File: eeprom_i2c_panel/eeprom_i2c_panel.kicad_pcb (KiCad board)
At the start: 2 copper layers, 69 x 91 mm, 28 parts, among them J1 Conn_01x03_Pin, J2 Conn_01x03_Pin, J3 Conn_01x03_Pin, J4 1x4 strip 2.54mm, U1 24LC256

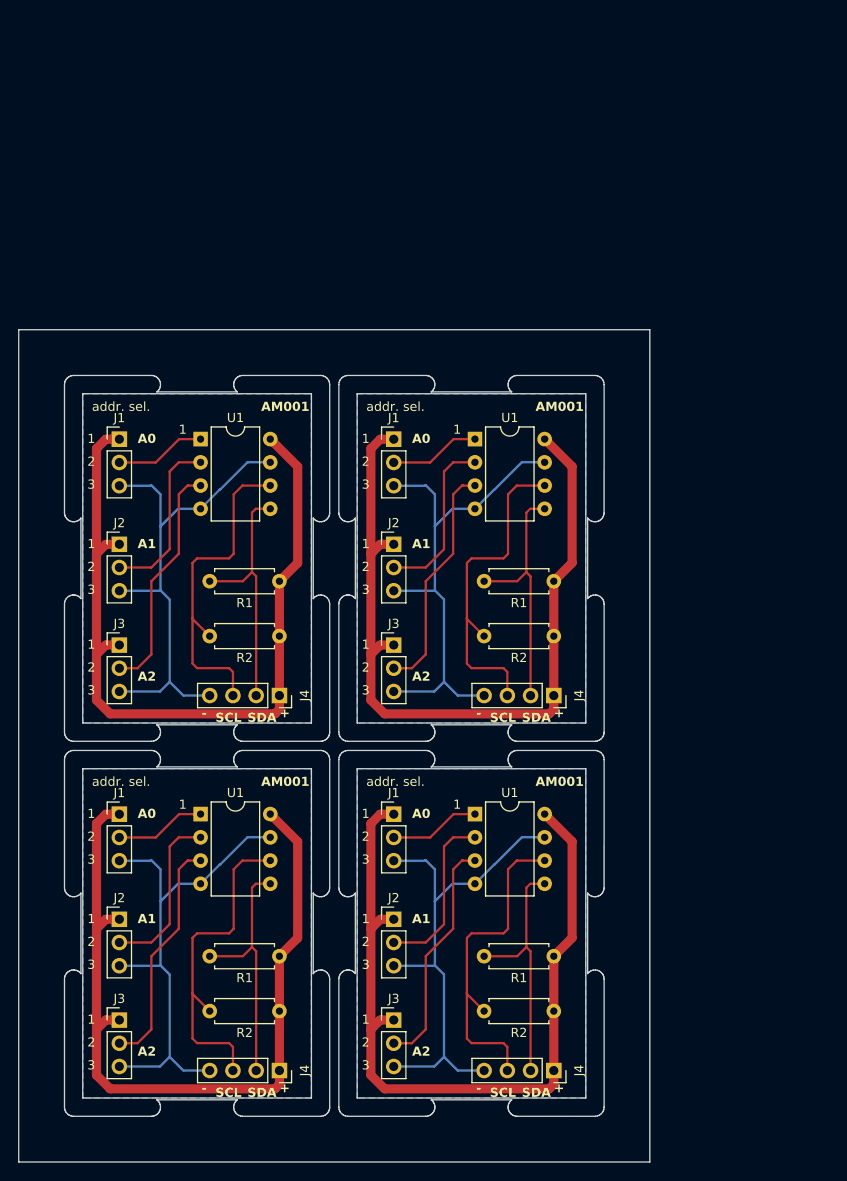
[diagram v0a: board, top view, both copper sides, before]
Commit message: Add by-pass capacitor; add mounting hole and change main connector's pinout.
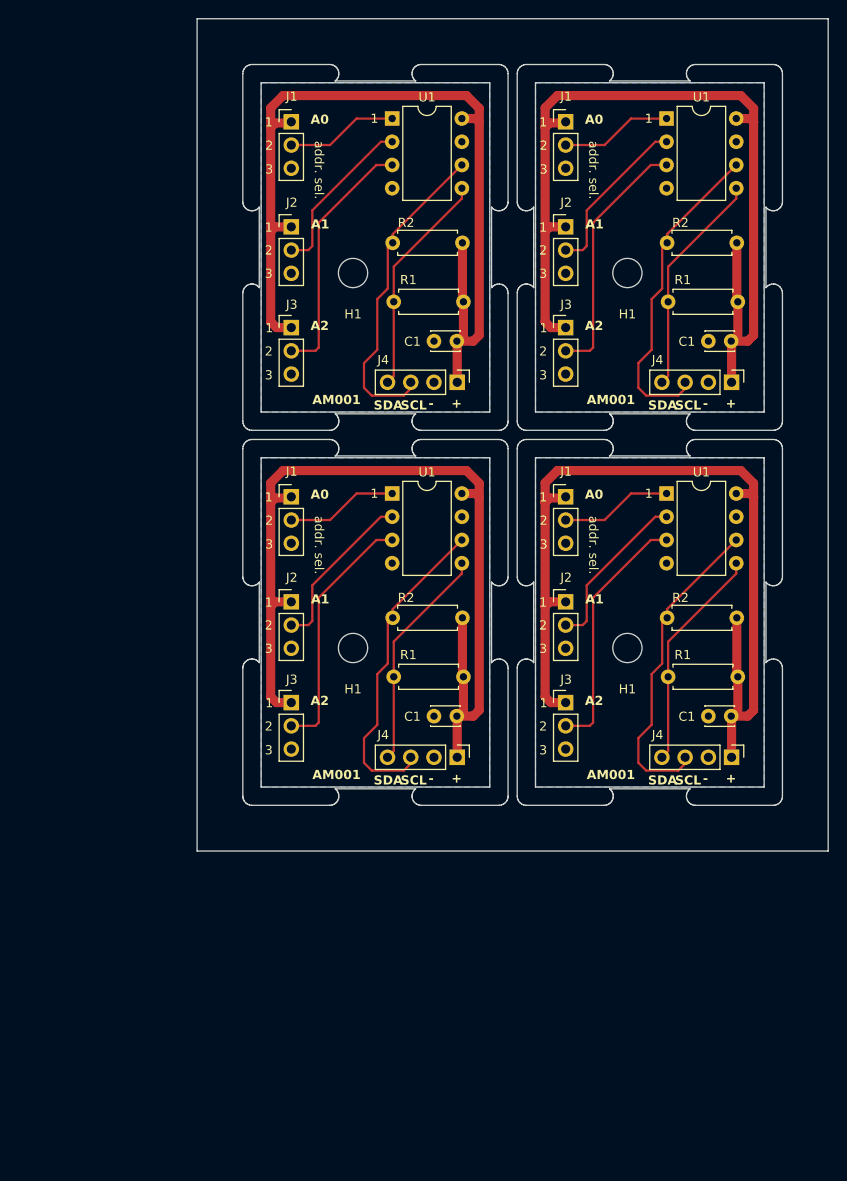
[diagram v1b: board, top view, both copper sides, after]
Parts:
- removed the J1 at (135.5, 66.0)
- removed the J1 at (105.5, 66.0)
- removed the J1 at (105.5, 107.0)
- removed the J1 at (135.5, 107.0)
- removed the J2 at (105.5, 77.5)
- removed the J2 at (135.5, 77.5)
- removed the J2 at (105.5, 118.5)
- removed the J2 at (135.5, 118.5)
- removed the J3 at (135.5, 129.5)
- removed the J3 at (105.5, 88.5)
- removed the J3 at (105.5, 129.5)
- removed the J3 at (135.5, 88.5)
- removed the J4 at (153.0, 94.0)
- removed the J4 at (123.0, 94.0)
- removed the J4 at (123.0, 135.0)
- removed the J4 at (153.0, 135.0)
- removed the R1 at (153.0, 81.5)
- removed the R1 at (153.0, 122.5)
- removed the R1 at (123.0, 81.5)
- removed the R1 at (123.0, 122.5)
- removed the R2 at (123.0, 87.5)
- removed the R2 at (153.0, 87.5)
- removed the R2 at (123.0, 128.5)
- removed the R2 at (153.0, 128.5)
- removed the U1 at (114.4, 66.0)
- removed the U1 at (144.4, 107.0)
- removed the U1 at (144.4, 66.0)
- removed the U1 at (114.4, 107.0)
- added C1: 100nf, Capacitor_THT:C_Disc_D3.0mm_W2.0mm_P2.50mm, F.Cu at (142.4, 96.2)
- added C1: 100nf, Capacitor_THT:C_Disc_D3.0mm_W2.0mm_P2.50mm, F.Cu at (142.4, 55.2)
- added C1: 100nf, Capacitor_THT:C_Disc_D3.0mm_W2.0mm_P2.50mm, F.Cu at (172.4, 96.2)
- added C1: 100nf, Capacitor_THT:C_Disc_D3.0mm_W2.0mm_P2.50mm, F.Cu at (172.4, 55.2)
- added H1: MountingHole, MountingHole:MountingHole_3.2mm_M3, F.Cu at (161.1, 88.8)
- added H1: MountingHole, MountingHole:MountingHole_3.2mm_M3, F.Cu at (131.1, 88.8)
- added H1: MountingHole, MountingHole:MountingHole_3.2mm_M3, F.Cu at (131.1, 47.8)
- added H1: MountingHole, MountingHole:MountingHole_3.2mm_M3, F.Cu at (161.1, 47.8)
- added J1: Conn_01x03_Pin, Connector_PinHeader_2.54mm:PinHeader_1x03_P2.54mm_Vertical, F.Cu at (154.3, 72.3)
- added J1: Conn_01x03_Pin, Connector_PinHeader_2.54mm:PinHeader_1x03_P2.54mm_Vertical, F.Cu at (124.3, 72.3)
- added J1: Conn_01x03_Pin, Connector_PinHeader_2.54mm:PinHeader_1x03_P2.54mm_Vertical, F.Cu at (124.3, 31.3)
- added J1: Conn_01x03_Pin, Connector_PinHeader_2.54mm:PinHeader_1x03_P2.54mm_Vertical, F.Cu at (154.3, 31.3)
- added J2: Conn_01x03_Pin, Connector_PinHeader_2.54mm:PinHeader_1x03_P2.54mm_Vertical, F.Cu at (154.3, 42.8)
- added J2: Conn_01x03_Pin, Connector_PinHeader_2.54mm:PinHeader_1x03_P2.54mm_Vertical, F.Cu at (124.3, 42.8)
- added J2: Conn_01x03_Pin, Connector_PinHeader_2.54mm:PinHeader_1x03_P2.54mm_Vertical, F.Cu at (124.3, 83.8)
- added J2: Conn_01x03_Pin, Connector_PinHeader_2.54mm:PinHeader_1x03_P2.54mm_Vertical, F.Cu at (154.3, 83.8)
- added J3: Conn_01x03_Pin, Connector_PinHeader_2.54mm:PinHeader_1x03_P2.54mm_Vertical, F.Cu at (154.3, 53.8)
- added J3: Conn_01x03_Pin, Connector_PinHeader_2.54mm:PinHeader_1x03_P2.54mm_Vertical, F.Cu at (154.3, 94.8)
- added J3: Conn_01x03_Pin, Connector_PinHeader_2.54mm:PinHeader_1x03_P2.54mm_Vertical, F.Cu at (124.3, 53.8)
- added J3: Conn_01x03_Pin, Connector_PinHeader_2.54mm:PinHeader_1x03_P2.54mm_Vertical, F.Cu at (124.3, 94.8)
- added J4: 1x4 strip 2.54mm, Connector_PinHeader_2.54mm:PinHeader_1x04_P2.54mm_Vertical, F.Cu at (142.4, 59.8)
- added J4: 1x4 strip 2.54mm, Connector_PinHeader_2.54mm:PinHeader_1x04_P2.54mm_Vertical, F.Cu at (142.4, 100.8)
- added J4: 1x4 strip 2.54mm, Connector_PinHeader_2.54mm:PinHeader_1x04_P2.54mm_Vertical, F.Cu at (172.4, 100.8)
- added J4: 1x4 strip 2.54mm, Connector_PinHeader_2.54mm:PinHeader_1x04_P2.54mm_Vertical, F.Cu at (172.4, 59.8)
- added R1: 2k0, Resistor_THT:R_Axial_DIN0207_L6.3mm_D2.5mm_P7.62mm_Horizontal, F.Cu at (143.1, 92.0)
- added R1: 2k0, Resistor_THT:R_Axial_DIN0207_L6.3mm_D2.5mm_P7.62mm_Horizontal, F.Cu at (143.1, 51.0)
- added R1: 2k0, Resistor_THT:R_Axial_DIN0207_L6.3mm_D2.5mm_P7.62mm_Horizontal, F.Cu at (173.1, 51.0)
- added R1: 2k0, Resistor_THT:R_Axial_DIN0207_L6.3mm_D2.5mm_P7.62mm_Horizontal, F.Cu at (173.1, 92.0)
- added R2: 2k0, Resistor_THT:R_Axial_DIN0207_L6.3mm_D2.5mm_P7.62mm_Horizontal, F.Cu at (173.0, 85.5)
- added R2: 2k0, Resistor_THT:R_Axial_DIN0207_L6.3mm_D2.5mm_P7.62mm_Horizontal, F.Cu at (143.0, 85.5)
- added R2: 2k0, Resistor_THT:R_Axial_DIN0207_L6.3mm_D2.5mm_P7.62mm_Horizontal, F.Cu at (143.0, 44.5)
- added R2: 2k0, Resistor_THT:R_Axial_DIN0207_L6.3mm_D2.5mm_P7.62mm_Horizontal, F.Cu at (173.0, 44.5)
- added U1: 24LC256, Package_DIP:DIP-8_W7.62mm, F.Cu at (165.3, 30.9)
- added U1: 24LC256, Package_DIP:DIP-8_W7.62mm, F.Cu at (165.3, 71.9)
- added U1: 24LC256, Package_DIP:DIP-8_W7.62mm, F.Cu at (135.3, 71.9)
- added U1: 24LC256, Package_DIP:DIP-8_W7.62mm, F.Cu at (135.3, 30.9)
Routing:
- net Board_3-Net-(J1-Pin_1): track 0.00 -> 99.9 mm
- net Board_0-Net-(J1-Pin_1): track 0.00 -> 99.9 mm
- net Board_2-Net-(J1-Pin_1): track 0.00 -> 99.9 mm
- net Board_1-Net-(J1-Pin_1): track 0.00 -> 99.9 mm
- net Board_2-VCC: track 88.7 -> 0.00 mm
- net Board_3-VCC: track 88.7 -> 0.00 mm
- net Board_1-VCC: track 88.7 -> 0.00 mm
- net Board_0-VCC: track 88.7 -> 0.00 mm
- net Board_2-GND: track 56.2 -> 0.00 mm
- net Board_1-GND: track 56.2 -> 0.00 mm
- net Board_0-GND: track 56.2 -> 0.00 mm
- net Board_3-GND: track 56.2 -> 0.00 mm
- net Board_3-Net-(J4-SDA): track 27.4 -> 24.6 mm
- net Board_1-Net-(J4-SDA): track 27.4 -> 24.6 mm
- net Board_0-Net-(J4-SDA): track 27.4 -> 24.6 mm
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
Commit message: Update panel for production and fix label position (gerber regenerated).
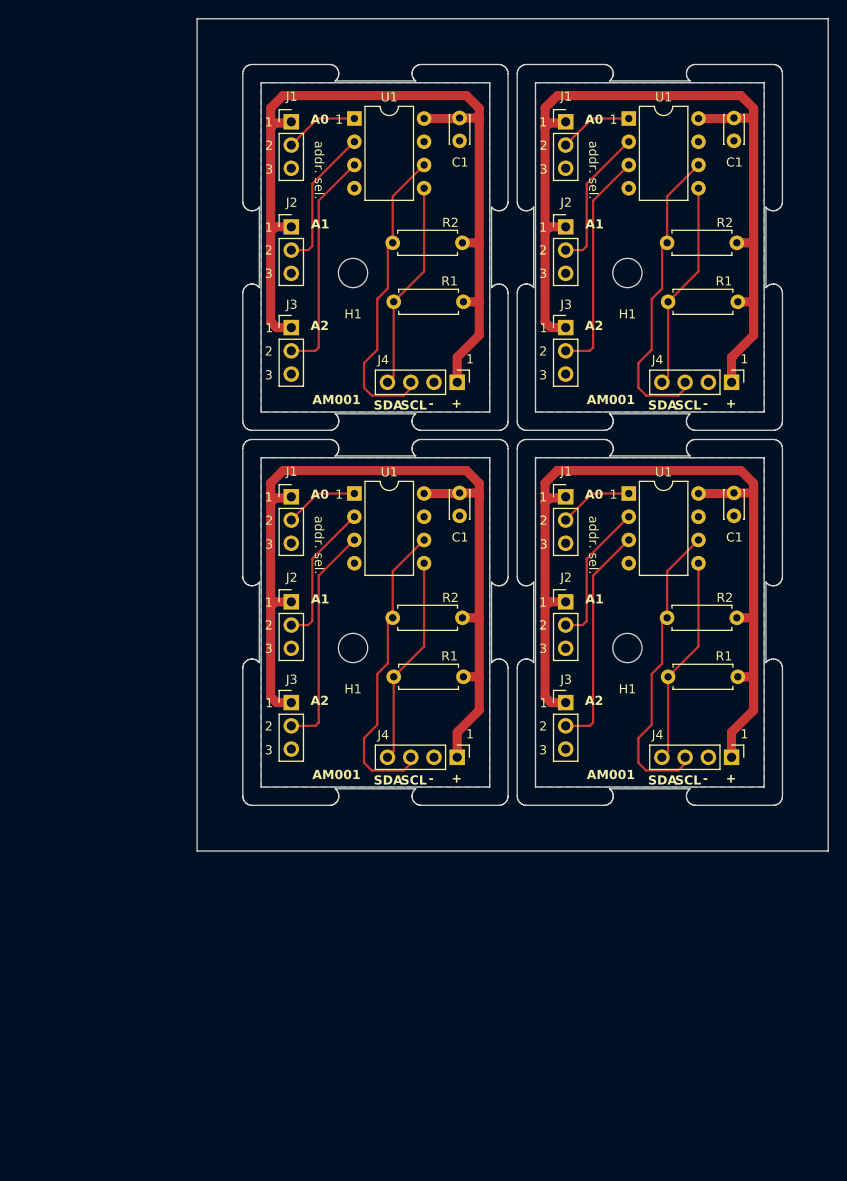
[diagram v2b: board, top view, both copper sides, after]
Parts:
- removed the C1 at (142.4, 96.2)
- removed the C1 at (142.4, 55.2)
- removed the C1 at (172.4, 96.2)
- removed the C1 at (172.4, 55.2)
- removed the U1 at (165.3, 30.9)
- removed the U1 at (165.3, 71.9)
- removed the U1 at (135.3, 71.9)
- removed the U1 at (135.3, 30.9)
- added C1: 100nf, Capacitor_THT:C_Disc_D3.0mm_W2.0mm_P2.50mm, F.Cu at (142.7, 71.8)
- added C1: 100nf, Capacitor_THT:C_Disc_D3.0mm_W2.0mm_P2.50mm, F.Cu at (142.7, 30.9)
- added C1: 100nf, Capacitor_THT:C_Disc_D3.0mm_W2.0mm_P2.50mm, F.Cu at (172.7, 30.9)
- added C1: 100nf, Capacitor_THT:C_Disc_D3.0mm_W2.0mm_P2.50mm, F.Cu at (172.7, 71.8)
- added U1: 24LC256, Package_DIP:DIP-8_W7.62mm, F.Cu at (131.2, 71.9)
- added U1: 24LC256, Package_DIP:DIP-8_W7.62mm, F.Cu at (131.2, 30.9)
- added U1: 24LC256, Package_DIP:DIP-8_W7.62mm, F.Cu at (161.2, 71.9)
- added U1: 24LC256, Package_DIP:DIP-8_W7.62mm, F.Cu at (161.2, 30.9)
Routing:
- net Board_3-Net-(J1-Pin_1): track 99.9 -> 95.6 mm
- net Board_2-Net-(J1-Pin_1): track 99.9 -> 95.6 mm
- net Board_1-Net-(J1-Pin_1): track 99.9 -> 95.6 mm
- net Board_0-Net-(J1-Pin_1): track 99.9 -> 95.6 mm
- net Board_2-Net-(J1-Pin_2): track 12.2 -> 8.10 mm
- net Board_0-Net-(J1-Pin_2): track 12.2 -> 8.10 mm
- net Board_1-Net-(J1-Pin_2): track 12.2 -> 8.10 mm
- net Board_3-Net-(J1-Pin_2): track 12.2 -> 8.10 mm
- net Board_1-Net-(J3-Pin_2): track 27.4 -> 24.7 mm
- net Board_3-Net-(J3-Pin_2): track 27.4 -> 24.7 mm
- net Board_2-Net-(J3-Pin_2): track 27.4 -> 24.7 mm
- net Board_0-Net-(J3-Pin_2): track 27.4 -> 24.7 mm
- net Board_1-Net-(J2-Pin_2): track 18.2 -> 15.8 mm
- net Board_3-Net-(J2-Pin_2): track 18.2 -> 15.8 mm
- net Board_0-Net-(J2-Pin_2): track 18.2 -> 15.8 mm
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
